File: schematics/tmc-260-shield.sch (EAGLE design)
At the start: 59 parts, among them IC1 TMC260-PA, J1 POWER_JACKPTH, Q1 BC856SOT323, T2 BC850SOT323, T3 BC850SOT323, T4 BC850SOT323

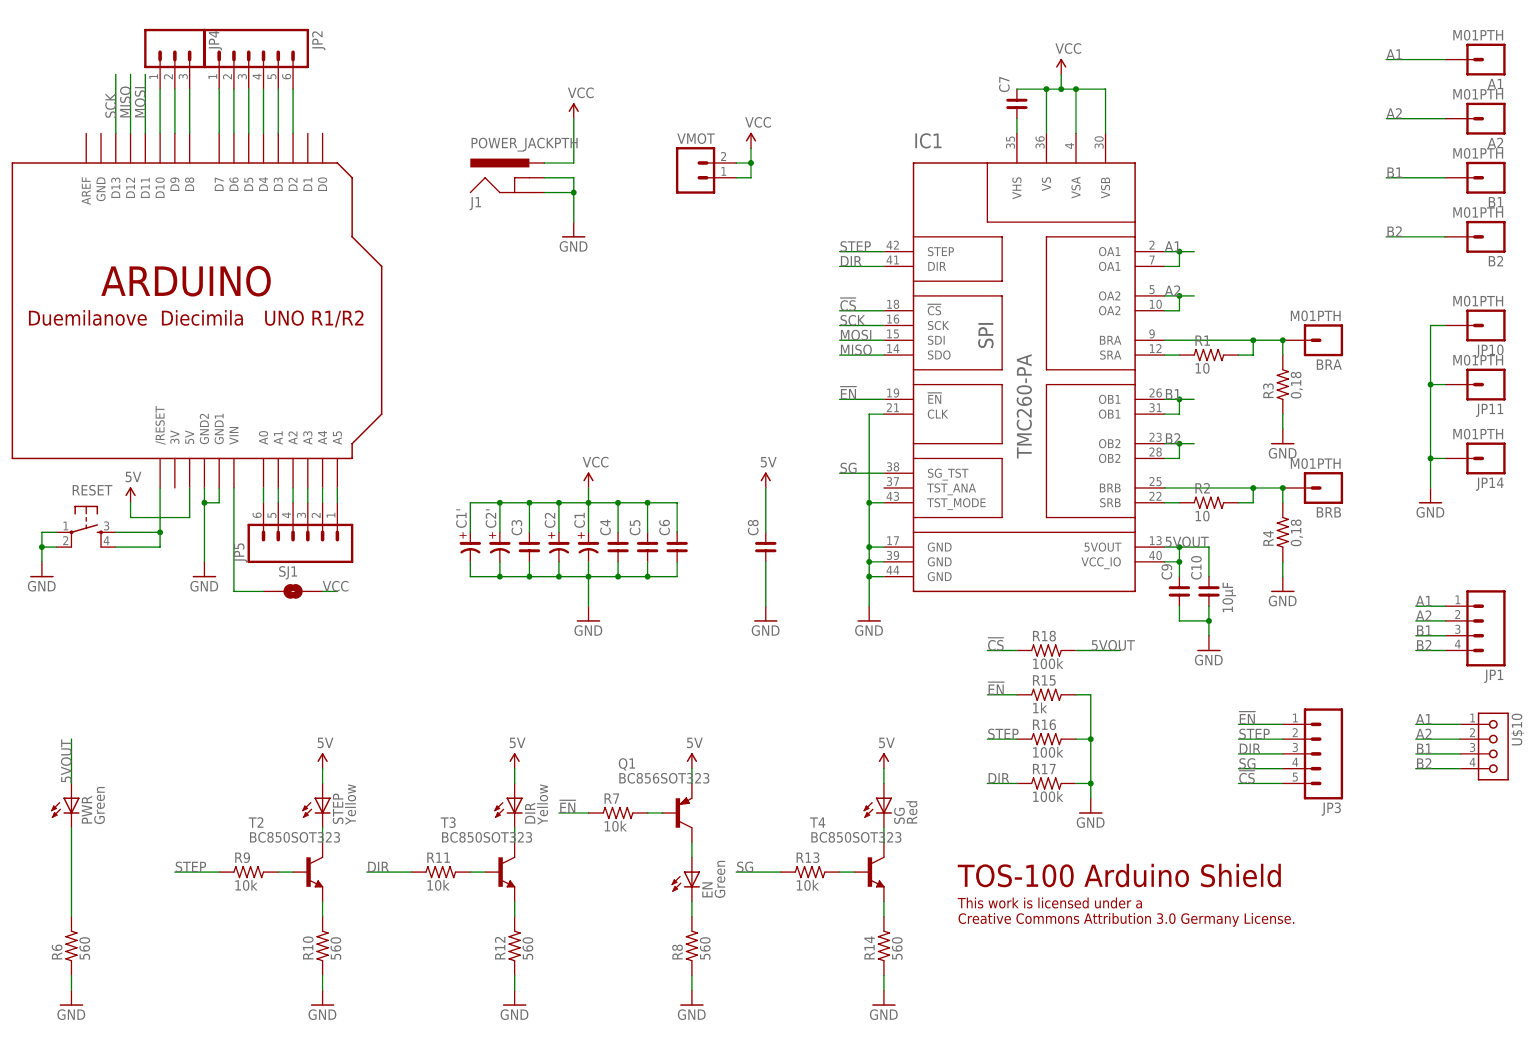
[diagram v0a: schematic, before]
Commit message: adding capacitor values
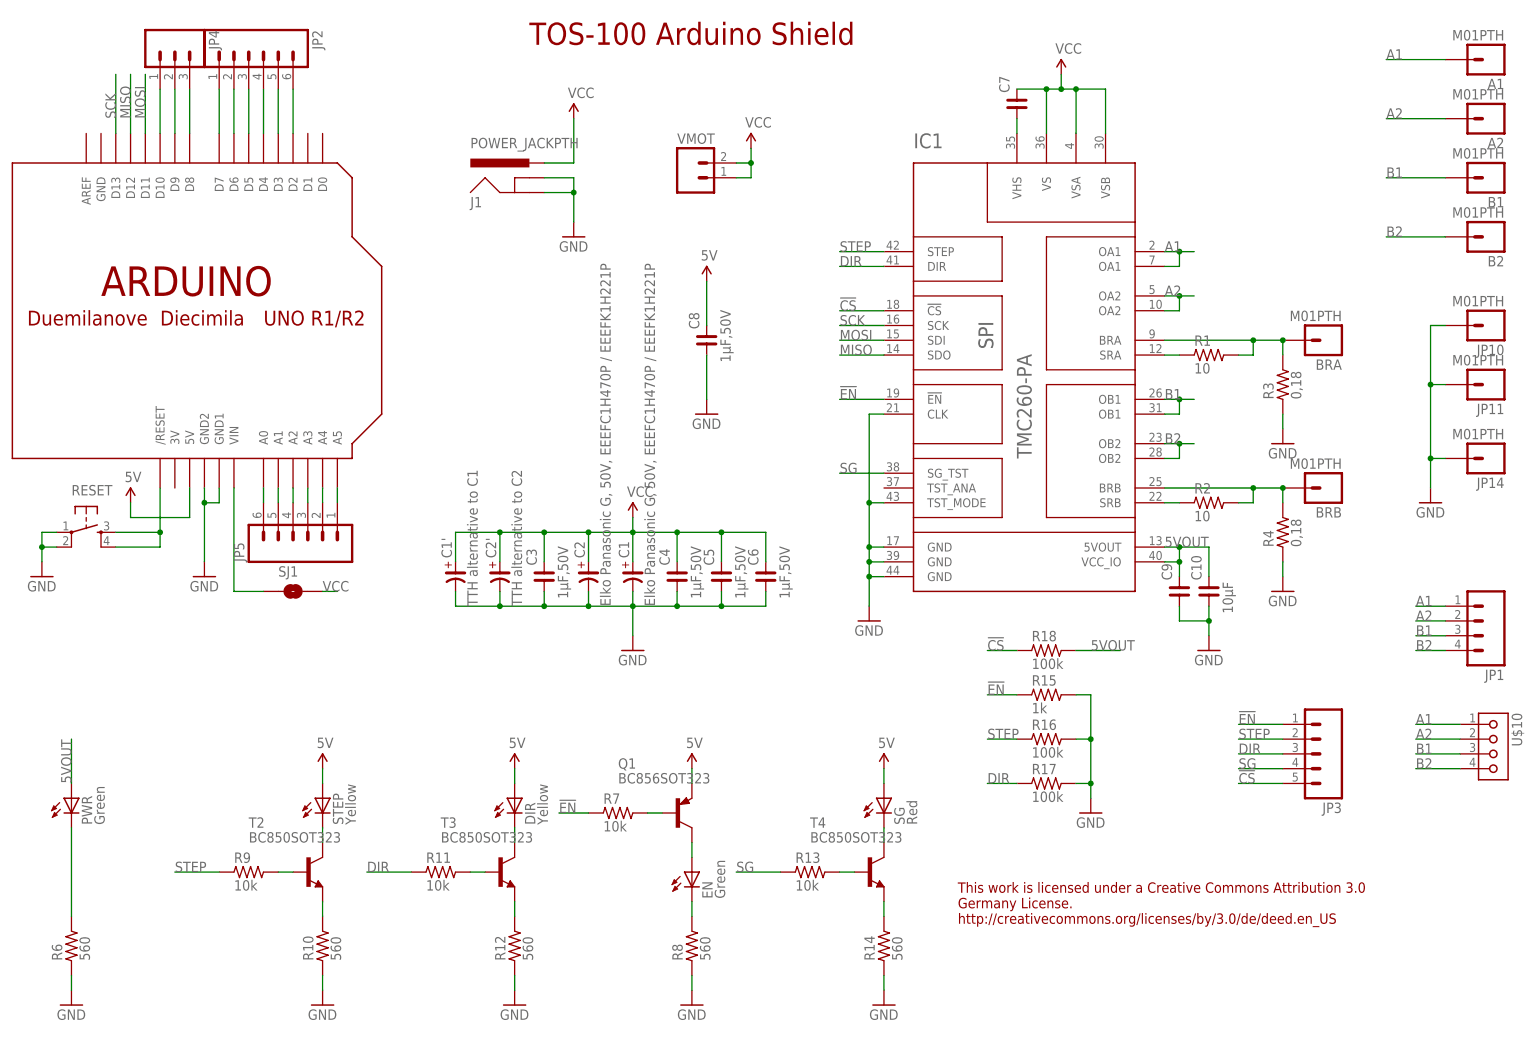
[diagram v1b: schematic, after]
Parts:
- C1, C2: value (none) -> Elko Panasonic G, 50V, EEEFC1H470P / EEEFK1H221P
- C1': value (none) -> TTH alternative to C1
- C2': value (none) -> TTH alternative to C2
- C3, C4, C5, C6, C8: value (none) -> 1µF,50V
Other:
- note added: "This work is licensed under a Creative Commons Attribution 3.0 Germany License. http://creativecommons.org/licenses/by/3.0/de/deed.en_US"
- note removed: "This work is licensed under a Creative Commons Attribution 3.0 Germany License."
- moved on the sheet: C1, C1', C2, C2', C3, C4, C5, C6, C8

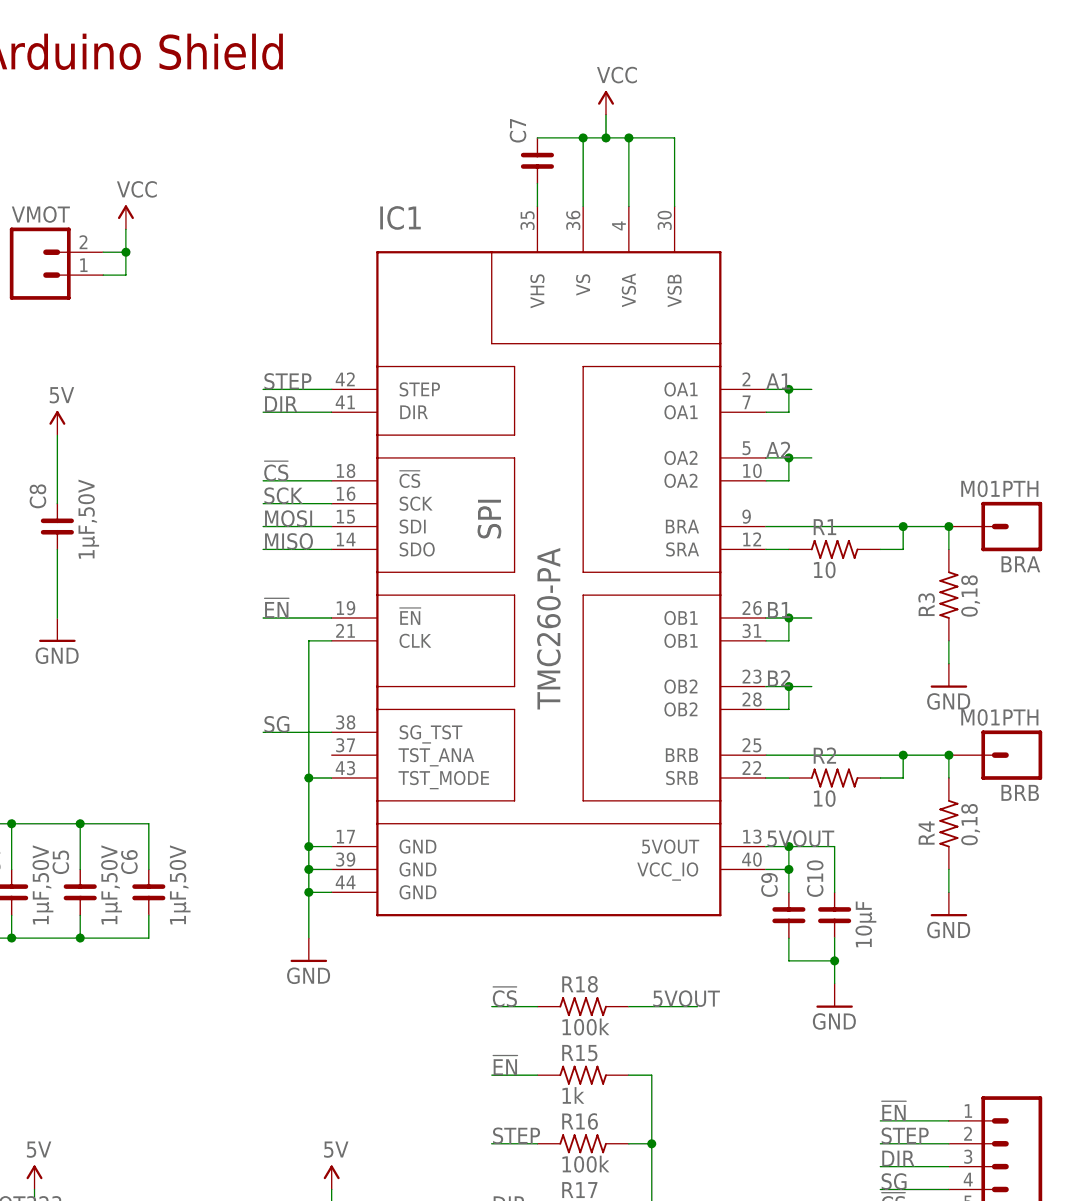
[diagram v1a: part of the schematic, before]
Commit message: Fixed some capacitor values
C6: changed value from 1µF to 10µF
C7: added value 1µF
C9: added value 1µF
C10: changed from 10µF to 1µF
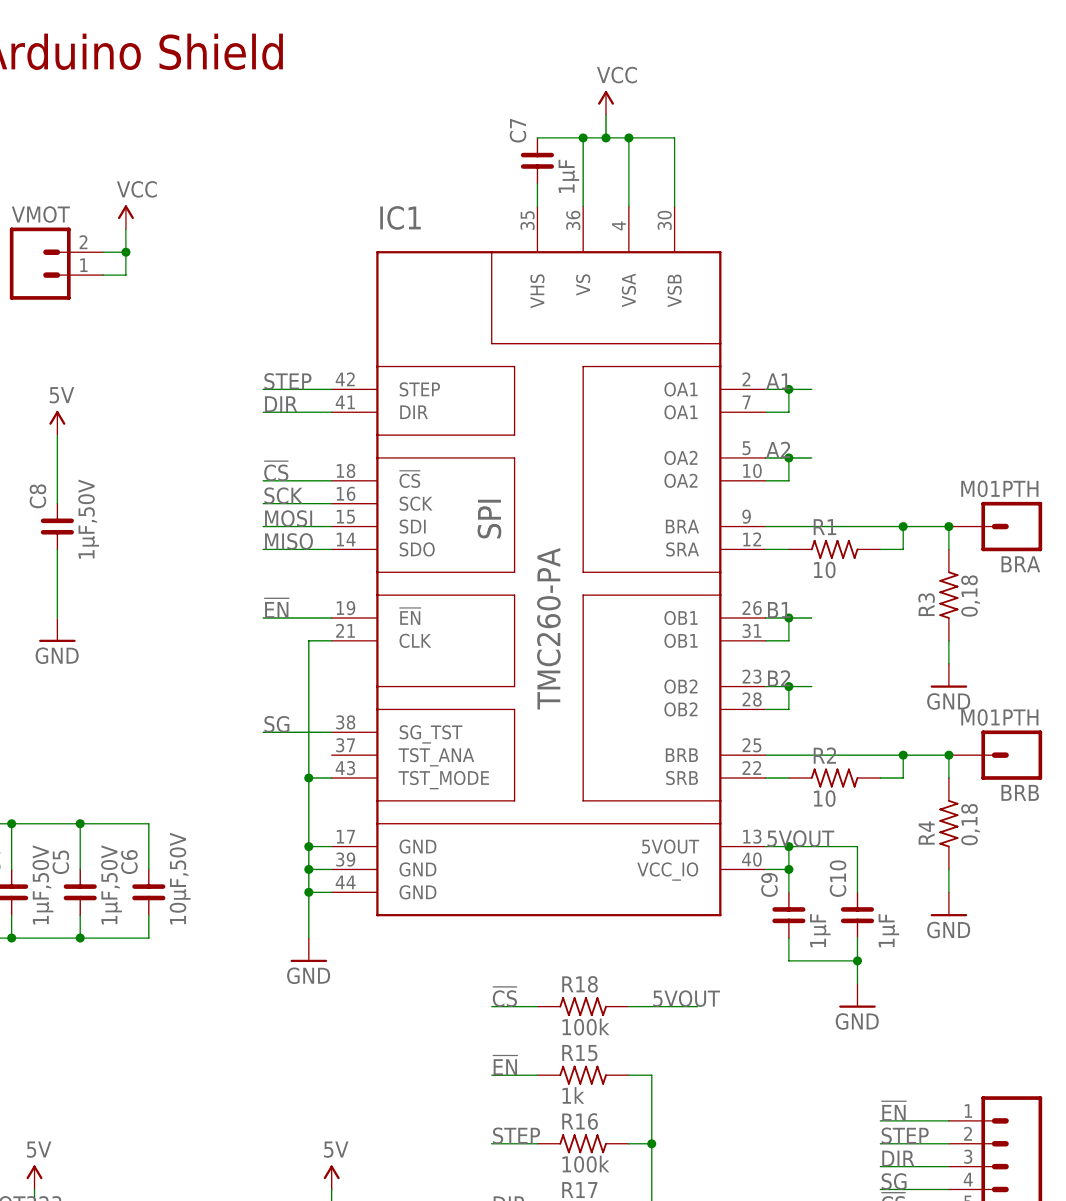
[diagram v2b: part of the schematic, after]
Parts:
- C10: value 10µF -> 1µF
- C6: value 1µF,50V -> 10µF,50V
- C7, C9: value (none) -> 1µF
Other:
- moved on the sheet: C10
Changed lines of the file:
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@@
 <part name="GND3" library="SparkFun" deviceset="GND" device=""/>
 <part name="P+2" library="SparkFun" deviceset="VCC" device=""/>
-<part name="C7" library="rc-master-smd" deviceset="C_" device="0603"/>
-<part name="C9" library="rc-master-smd" deviceset="C_" device="0603"/>
-<part name="C10" library="rc-master-smd" deviceset="C_" device="0603" value="10µF"/>
+<part name="C7" library="rc-master-smd" deviceset="C_" device="0603" value="1µF"/>
+<part name="C9" library="rc-master-smd" deviceset="C_" device="0603" value="1µF"/>
+<part name="C10" library="rc-master-smd" deviceset="C_" device="0603" value="1µF"/>
 <part name="GND4" library="SparkFun" deviceset="GND" device=""/>
 <part name="GND5" library="SparkFun" deviceset="GND" device=""/>
@@
 <part name="C4" library="rc-master-smd" deviceset="C_" device="0603" value="1µF,50V"/>
 <part name="C5" library="rc-master-smd" deviceset="C_" device="0603" value="1µF,50V"/>
-<part name="C6" library="rc-master-smd" deviceset="C_" device="1206" value="1µF,50V"/>
+<part name="C6" library="rc-master-smd" deviceset="C_" device="1206" value="10µF,50V"/>
 <part name="VMOT" library="SparkFun" deviceset="M02" device="1X02_NO_SILK"/>
 <part name="P+4" library="SparkFun" deviceset="VCC" device=""/>
@@
 <instance part="C7" gate="G$1" x="175.26" y="165.1" rot="R90"/>
 <instance part="C9" gate="G$1" x="203.2" y="81.28" rot="R90"/>
-<instance part="C10" gate="G$1" x="208.28" y="81.28" rot="R90"/>
+<instance part="C10" gate="G$1" x="210.82" y="81.28" rot="R90"/>
 <instance part="GND4" gate="1" x="149.86" y="76.2"/>
-<instance part="GND5" gate="1" x="208.28" y="71.12"/>
+<instance part="GND5" gate="1" x="210.82" y="71.12"/>
 <instance part="GND6" gate="1" x="35.56" y="83.82"/>
 <instance part="RESET" gate="S" x="15.24" y="91.44"/>
@@
 <segment>
 <wire x1="203.2" y1="78.74" x2="203.2" y2="76.2" width="0.1524" layer="91"/>
-<wire x1="203.2" y1="76.2" x2="208.28" y2="76.2" width="0.1524" layer="91"/>
-<wire x1="208.28" y1="76.2" x2="208.28" y2="78.74" width="0.1524" layer="91"/>
-<wire x1="208.28" y1="76.2" x2="208.28" y2="73.66" width="0.1524" layer="91"/>
-<junction x="208.28" y="76.2"/>
+<wire x1="203.2" y1="76.2" x2="210.82" y2="76.2" width="0.1524" layer="91"/>
+<wire x1="210.82" y1="76.2" x2="210.82" y2="78.74" width="0.1524" layer="91"/>
+<wire x1="210.82" y1="76.2" x2="210.82" y2="73.66" width="0.1524" layer="91"/>
+<junction x="210.82" y="76.2"/>
 <pinref part="C9" gate="G$1" pin="1"/>
 <pinref part="C10" gate="G$1" pin="1"/>
@@
 <segment>
 <wire x1="200.66" y1="88.9" x2="203.2" y2="88.9" width="0.1524" layer="91"/>
-<wire x1="203.2" y1="88.9" x2="208.28" y2="88.9" width="0.1524" layer="91"/>
-<wire x1="208.28" y1="88.9" x2="208.28" y2="83.82" width="0.1524" layer="91"/>
+<wire x1="203.2" y1="88.9" x2="210.82" y2="88.9" width="0.1524" layer="91"/>
+<wire x1="210.82" y1="88.9" x2="210.82" y2="83.82" width="0.1524" layer="91"/>
 <wire x1="200.66" y1="86.36" x2="203.2" y2="86.36" width="0.1524" layer="91"/>
 <wire x1="203.2" y1="86.36" x2="203.2" y2="83.82" width="0.1524" layer="91"/>
